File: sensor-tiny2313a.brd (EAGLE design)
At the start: 54 x 39 mm, 36 parts, among them IC1 TINY2313-*S*, M1 NRF24L01P-M, M2 DHT22-NP, Q2 IRLML2502, U1 MCP1640C, X1 I2C, X2 serial

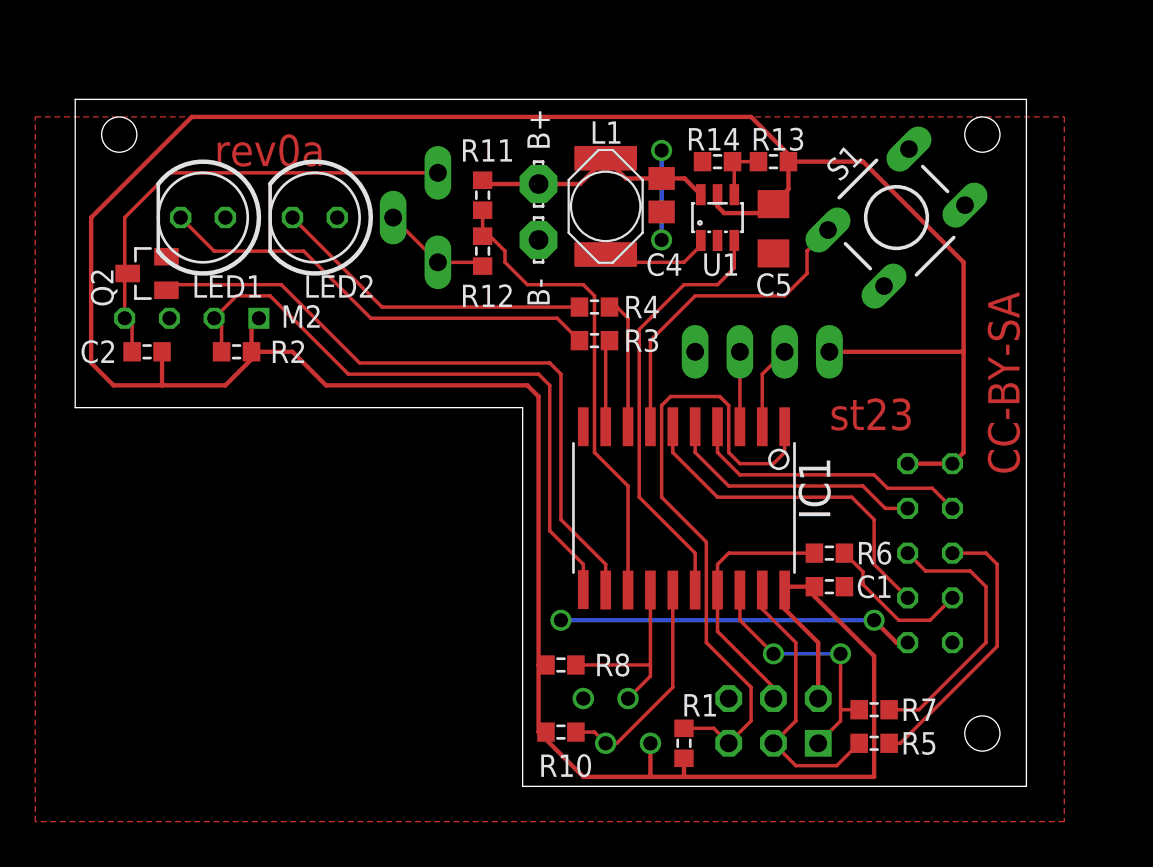
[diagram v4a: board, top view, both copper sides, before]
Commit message: renamed ic1->u1, u1->u2
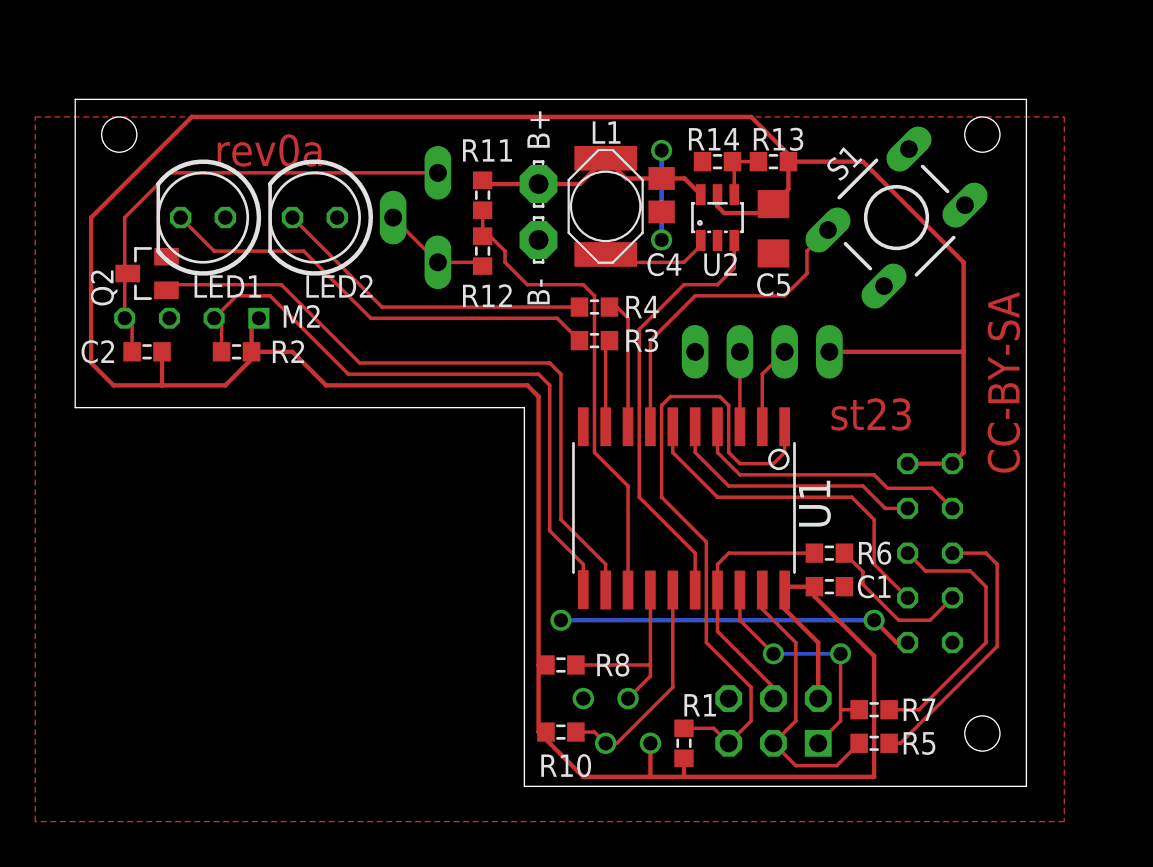
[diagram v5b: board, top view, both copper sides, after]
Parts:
- removed IC1: TINY2313-*S*, avr-7:SO20L$
- added U2: MCP1640C, karlnet-parts:SOT23-6
- U1: value MCP1640C -> TINY2313-*S*; device karlnet-parts:SOT23-6 -> avr-7:SO20L$
- moved U1 16.6 mm to (35.6, 17.8), turned to 180 degrees
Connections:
- net !RESET: now also U1.1; no longer IC1.1
- net AIN1: now also U1.13; no longer IC1.13
- net DHTON: now also U1.12; no longer IC1.12
- net DI: now also U1.17; no longer IC1.17
- net DO: now also U1.18; no longer IC1.18
- net GND: now also U1.10, U2.2; no longer IC1.10, U1.2
- net ICP1: now also U1.11; no longer IC1.11
- net LED1: now also U1.9; no longer IC1.9
- net LED2: now also U1.8; no longer IC1.8
- net N$8: now also U2.1; no longer U1.1
- net N$9: now also U2.4; no longer U1.4
- net PWRON: now also U1.16, U2.3; no longer IC1.16, U1.3
- net RFCE: now also U1.4; no longer IC1.4
- net RFCSN: now also U1.5; no longer IC1.5
- net RFIRQ: now also U1.6; no longer IC1.6
- net RXD: now also U1.2; no longer IC1.2
- net SCK: now also U1.19; no longer IC1.19
- net SCL: now also U1.15; no longer IC1.15
- net SDA: now also U1.14; no longer IC1.14
- net SW1: now also U1.7; no longer IC1.7
- net TXD: now also U1.3; no longer IC1.3
- net VBAT: now also U2.6; no longer U1.6
- net VCC: now also U1.20, U2.5; no longer IC1.20, U1.5
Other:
- outline, holes or cut-outs redrawn
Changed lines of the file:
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@@
 <layer number="44" name="Drills" color="7" fill="1" visible="no" active="yes"/>
 <layer number="45" name="Holes" color="7" fill="1" visible="no" active="yes"/>
-<layer number="46" name="Milling" color="3" fill="1" visible="no" active="yes"/>
+<layer number="46" name="Milling" color="3" fill="1" visible="yes" active="yes"/>
 <layer number="47" name="Measures" color="7" fill="1" visible="no" active="yes"/>
 <layer number="48" name="Document" color="7" fill="1" visible="no" active="yes"/>
@@
 <board>
 <plain>
-<wire x1="26.4" y1="2" x2="55" y2="2" width="0" layer="20"/>
+<wire x1="26.5" y1="2" x2="55" y2="2" width="0" layer="20"/>
 <wire x1="55" y1="2" x2="55" y2="41" width="0" layer="20"/>
 <wire x1="55" y1="41" x2="1" y2="41" width="0" layer="20"/>
 <wire x1="1" y1="41" x2="1" y2="23.5" width="0" layer="20"/>
-<wire x1="1" y1="23.5" x2="26.4" y2="23.5" width="0" layer="20"/>
-<wire x1="26.4" y1="23.5" x2="26.4" y2="2" width="0" layer="20"/>
+<wire x1="1" y1="23.5" x2="26.5" y2="23.5" width="0" layer="20"/>
+<wire x1="26.5" y1="23.5" x2="26.5" y2="2" width="0" layer="20"/>
 <hole x="52.5" y="5" drill="2"/>
 <hole x="52.5" y="39" drill="2"/>
@@
 <attribute name="VALUE" x="46.99" y="8.89" size="1.27" layer="27" rot="R180"/>
 </element>
-<element name="IC1" library="avr-7" package="SO20L$" value="TINY2313-*S*" x="35.56" y="17.78" smashed="yes" rot="R180">
-<attribute name="NAME" x="42.0878" y="20.701" size="1.778" layer="25" ratio="10" rot="R270"/>
+<element name="U1" library="avr-7" package="SO20L$" value="TINY2313-*S*" x="35.56" y="17.78" smashed="yes" rot="R180">
+<attribute name="NAME" x="42.0878" y="19.558" size="1.778" layer="25" ratio="10" rot="R270"/>
 <attribute name="VALUE" x="45.72" y="18.542" size="1.778" layer="27" ratio="10" rot="R180"/>
 </element>
@@
 <attribute name="VALUE" x="27.051" y="36.195" size="0.0254" layer="27" rot="R90"/>
 </element>
-<element name="U1" library="karlnet-parts" package="SOT23-6" value="MCP1640C" x="37.465" y="34.29" smashed="yes">
+<element name="U2" library="karlnet-parts" package="SOT23-6" value="MCP1640C" x="37.465" y="34.29" smashed="yes">
 <attribute name="NAME" x="36.576" y="30.988" size="1.27" layer="25"/>
 <attribute name="VALUE" x="35.56" y="30.861" size="1.27" layer="27"/>
@@
 <signals>
 <signal name="SCK">
-<contactref element="IC1" pad="19"/>
+<contactref element="U1" pad="19"/>
 <contactref element="R5" pad="1"/>
 <contactref element="ISP" pad="3"/>
@@
 <contactref element="C1" pad="2"/>
 <contactref element="ISP" pad="6"/>
-<contactref element="IC1" pad="10"/>
+<contactref element="U1" pad="10"/>
 <contactref element="S1" pad="3"/>
-<contactref element="IC1" pad="10"/>
+<contactref element="U1" pad="10"/>
 <contactref element="M1" pad="GND_A"/>
 <contactref element="M1" pad="GND_B"/>
@@
 <vertex x="-1.27" y="0"/>
 </polygon>
-<contactref element="U1" pad="2"/>
+<contactref element="U2" pad="2"/>
 <contactref element="C4" pad="2"/>
 <contactref element="B-" pad="MP"/>
@@
 <contactref element="ISP" pad="2"/>
 <contactref element="C1" pad="1"/>
-<contactref element="IC1" pad="20"/>
-<contactref element="IC1" pad="20"/>
+<contactref element="U1" pad="20"/>
+<contactref element="U1" pad="20"/>
 <contactref element="M1" pad="VCC_B"/>
 <contactref element="M1" pad="VCC_A"/>
 <contactref element="M1" pad="VCC_B"/>
 <contactref element="M1" pad="VCC_A"/>
-<contactref element="U1" pad="5"/>
+<contactref element="U2" pad="5"/>
 <contactref element="C5" pad="1"/>
 <contactref element="R13" pad="1"/>
@@
 <signal name="DHTON">
 <contactref element="Q2" pad="1"/>
-<contactref element="IC1" pad="12"/>
+<contactref element="U1" pad="12"/>
 <wire x1="28.575" y1="17.145" x2="31.115" y2="14.605" width="0.2" layer="1"/>
 <wire x1="31.115" y1="14.605" x2="31.115" y2="13.1445" width="0.2" layer="1"/>
@@
 </signal>
 <signal name="AIN1">
-<contactref element="IC1" pad="13"/>
+<contactref element="U1" pad="13"/>
 <contactref element="R11" pad="2"/>
 <contactref element="R12" pad="1"/>
@@
 </signal>
 <signal name="!RESET">
-<contactref element="IC1" pad="1"/>
+<contactref element="U1" pad="1"/>
 <contactref element="R1" pad="2"/>
 <contactref element="ISP" pad="5"/>
@@
 <signal name="RFCE">
 <contactref element="M1" pad="CE"/>
-<contactref element="IC1" pad="4"/>
+<contactref element="U1" pad="4"/>
 <wire x1="50.8" y1="17.78" x2="49.657" y2="18.923" width="0.2" layer="1"/>
 <wire x1="49.657" y1="18.923" x2="47.117" y2="18.923" width="0.2" layer="1"/>
@@
 </signal>
 <signal name="LED1">
-<contactref element="IC1" pad="9"/>
+<contactref element="U1" pad="9"/>
 <contactref element="R3" pad="1"/>
 <wire x1="31.115" y1="22.4155" x2="31.115" y2="27.09" width="0.2" layer="1"/>
@@
 <signal name="ICP1">
 <contactref element="R2" pad="2"/>
-<contactref element="IC1" pad="11"/>
+<contactref element="U1" pad="11"/>
 <contactref element="M2" pad="2"/>
 <wire x1="8.89" y1="28.575" x2="9.31" y2="28.155" width="0.2" layer="1"/>
@@
 </signal>
 <signal name="DO">
-<contactref element="IC1" pad="18"/>
+<contactref element="U1" pad="18"/>
 <contactref element="R7" pad="2"/>
 <contactref element="ISP" pad="1"/>
@@
 </signal>
 <signal name="DI">
-<contactref element="IC1" pad="17"/>
+<contactref element="U1" pad="17"/>
 <contactref element="R6" pad="1"/>
 <contactref element="ISP" pad="4"/>
@@
 <signal name="RFCSN">
 <contactref element="M1" pad="CSN"/>
-<contactref element="IC1" pad="5"/>
+<contactref element="U1" pad="5"/>
 <wire x1="48.26" y1="17.78" x2="46.99" y2="17.78" width="0.2" layer="1"/>
 <wire x1="46.99" y1="17.78" x2="45.72" y2="19.05" width="0.2" layer="1"/>
@@
 </signal>
 <signal name="SW1">
-<contactref element="IC1" pad="7"/>
+<contactref element="U1" pad="7"/>
 <contactref element="S1" pad="1"/>
 <wire x1="33.655" y1="22.4155" x2="33.655" y2="27.305" width="0.2" layer="1"/>
@@
 <signal name="N$8">
 <contactref element="L1" pad="1"/>
-<contactref element="U1" pad="1"/>
+<contactref element="U2" pad="1"/>
 <wire x1="36.515" y1="32.99" x2="36.515" y2="32.705" width="0.2" layer="1"/>
 <wire x1="36.515" y1="32.705" x2="35.56" y2="31.75" width="0.2" layer="1"/>
@@
 <contactref element="R13" pad="2"/>
 <contactref element="R14" pad="2"/>
-<contactref element="U1" pad="4"/>
+<contactref element="U2" pad="4"/>
 <wire x1="38.415" y1="35.59" x2="38.415" y2="37.365" width="0.2" layer="1"/>
 <wire x1="38.415" y1="37.365" x2="38.315" y2="37.465" width="0.2" layer="1"/>
@@
 </signal>
 <signal name="VBAT" class="1">
-<contactref element="U1" pad="6"/>
+<contactref element="U2" pad="6"/>
 <contactref element="L1" pad="2"/>
 <contactref element="C4" pad="1"/>
@@
 </signal>
 <signal name="PWRON">
-<contactref element="U1" pad="3"/>
-<contactref element="IC1" pad="16"/>
+<contactref element="U2" pad="3"/>
+<contactref element="U1" pad="16"/>
 <wire x1="38.415" y1="32.99" x2="38.415" y2="31.43" width="0.2" layer="1"/>
 <wire x1="33.02" y1="18.415" x2="36.195" y2="15.24" width="0.2" layer="1"/>
@@
 <signal name="RFIRQ">
 <contactref element="M1" pad="IRQ"/>
-<contactref element="IC1" pad="6"/>
+<contactref element="U1" pad="6"/>
 <wire x1="45.085" y1="18.415" x2="37.465" y2="18.415" width="0.2" layer="1"/>
 <wire x1="45.085" y1="18.415" x2="46.355" y2="17.145" width="0.2" layer="1"/>
@@
 </signal>
 <signal name="LED2">
-<contactref element="IC1" pad="8"/>
+<contactref element="U1" pad="8"/>
 <contactref element="R4" pad="1"/>
 <wire x1="32.385" y1="22.4155" x2="32.385" y2="28.575" width="0.2" layer="1"/>
@@
 </signal>
 <signal name="TXD">
-<contactref element="IC1" pad="3"/>
+<contactref element="U1" pad="3"/>
 <contactref element="X2" pad="3"/>
 <wire x1="38.735" y1="22.4155" x2="38.735" y2="26.67" width="0.2" layer="1"/>
 </signal>
 <signal name="RXD">
-<contactref element="IC1" pad="2"/>
+<contactref element="U1" pad="2"/>
 <contactref element="X2" pad="2"/>
 <wire x1="40.005" y1="22.4155" x2="40.005" y2="25.4" width="0.2" layer="1"/>
@@
 </signal>
 <signal name="SDA">
-<contactref element="IC1" pad="14"/>
+<contactref element="U1" pad="14"/>
 <contactref element="R8" pad="2"/>
 <contactref element="X1" pad="2"/>
@@
 </signal>
 <signal name="SCL">
-<contactref element="IC1" pad="15"/>
+<contactref element="U1" pad="15"/>
 <contactref element="R10" pad="2"/>
 <contactref element="X1" pad="3"/>
@@
 </signal>
 </signals>
-<errors>
-</errors>
 </board>
 </drawing>

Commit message: gnd plane reshaped
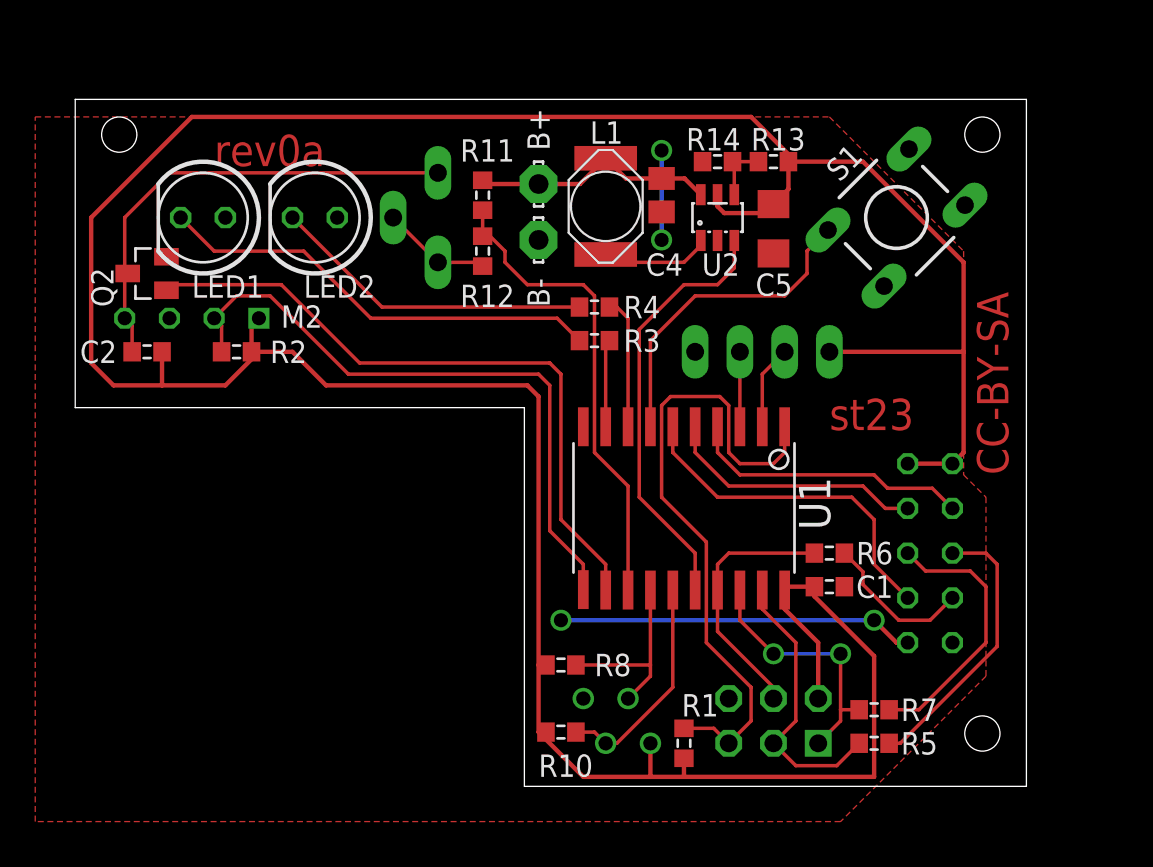
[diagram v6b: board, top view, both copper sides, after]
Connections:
- net GND: no longer S1.4
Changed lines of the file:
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@@
 <layer number="14" name="Route14" color="1" fill="6" visible="no" active="no"/>
 <layer number="15" name="Route15" color="4" fill="6" visible="no" active="no"/>
-<layer number="16" name="Bottom" color="1" fill="1" visible="no" active="yes"/>
+<layer number="16" name="Bottom" color="1" fill="1" visible="yes" active="yes"/>
 <layer number="17" name="Pads" color="2" fill="1" visible="yes" active="yes"/>
 <layer number="18" name="Vias" color="2" fill="1" visible="yes" active="yes"/>
@@
 <layer number="20" name="Dimension" color="15" fill="1" visible="yes" active="yes"/>
 <layer number="21" name="tPlace" color="7" fill="1" visible="yes" active="yes"/>
-<layer number="22" name="bPlace" color="7" fill="1" visible="no" active="yes"/>
+<layer number="22" name="bPlace" color="7" fill="1" visible="yes" active="yes"/>
 <layer number="23" name="tOrigins" color="15" fill="1" visible="yes" active="yes"/>
-<layer number="24" name="bOrigins" color="15" fill="1" visible="no" active="yes"/>
+<layer number="24" name="bOrigins" color="15" fill="1" visible="yes" active="yes"/>
 <layer number="25" name="tNames" color="7" fill="1" visible="yes" active="yes"/>
 <layer number="26" name="bNames" color="7" fill="1" visible="no" active="yes"/>
@@
 <text x="43.815" y="22.225" size="1.778" layer="1" font="vector" ratio="12">&gt;BN</text>
 <text x="8.89" y="37.211" size="1.778" layer="1" ratio="12">&gt;BR</text>
-<text x="54.61" y="19.685" size="1.778" layer="1" ratio="12" rot="R90">CC-BY-SA</text>
+<text x="53.975" y="19.685" size="1.778" layer="1" ratio="12" rot="R90">CC-BY-SA</text>
 <dimension x1="1" y1="41" x2="0.6" y2="23.5" x3="-5.2" y3="32.25" textsize="1.778" textratio="12" layer="47" dtype="vertical"/>
 <dimension x1="26.4" y1="2" x2="26.4" y2="23.5" x3="-9.6" y3="12.75" textsize="1.778" textratio="12" layer="47" dtype="vertical"/>
@@
 <polygon width="0.25" layer="1">
 <vertex x="-1.27" y="40.005"/>
-<vertex x="57.15" y="40.005"/>
-<vertex x="57.15" y="0"/>
+<vertex x="43.815" y="40.005"/>
+<vertex x="51.435" y="32.385"/>
+<vertex x="51.435" y="19.685"/>
+<vertex x="52.705" y="18.415"/>
+<vertex x="52.705" y="8.255"/>
+<vertex x="44.45" y="0"/>
 <vertex x="-1.27" y="0"/>
 </polygon>
@@
 <wire x1="46.355" y1="11.43" x2="28.575" y2="11.43" width="0.25" layer="16"/>
 <via x="28.575" y="11.43" extent="1-16" drill="0.8" shape="octagon"/>
-<contactref element="S1" pad="4"/>
 </signal>
 <signal name="VCC" class="1">

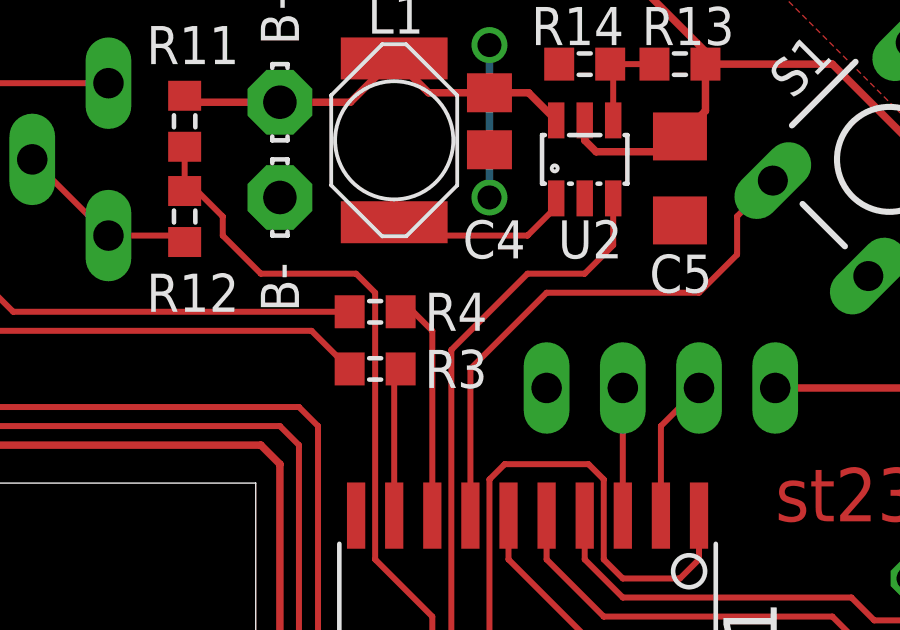
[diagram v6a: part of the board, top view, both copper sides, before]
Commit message: pulldown for boostup enable line
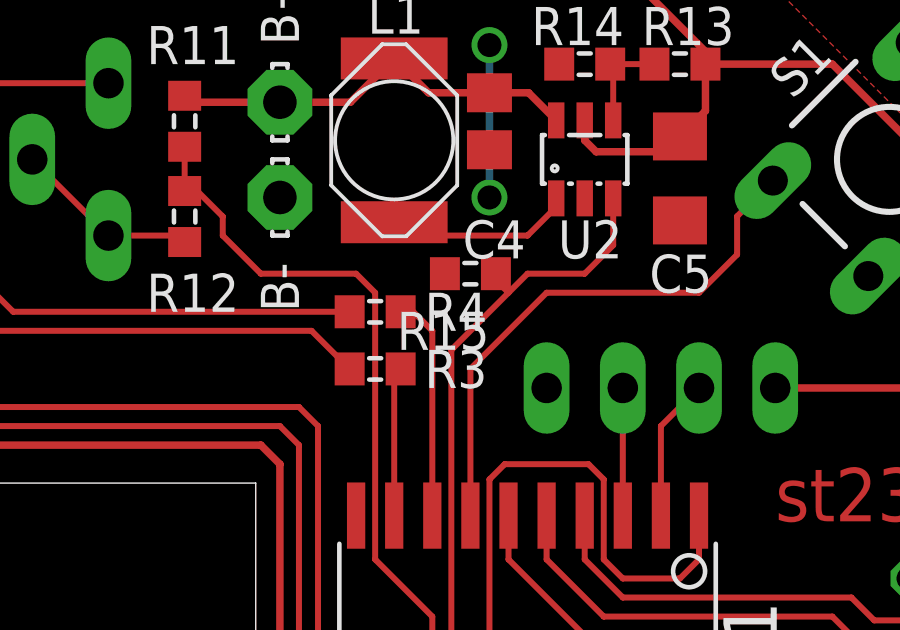
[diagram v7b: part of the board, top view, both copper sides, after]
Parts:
- added R15: 10k, rcl:R0603
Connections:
- net GND: now also R15.2
- net PWRON: now also R15.1
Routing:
- net PWRON: track 24.5 -> 25.6 mm
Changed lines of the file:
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@@
 <setting verticaltext="up"/>
 </settings>
-<grid distance="0.635" unitdist="mm" unit="mm" style="lines" multiple="1" display="yes" altdistance="5" altunitdist="mil" altunit="mic"/>
+<grid distance="0.635" unitdist="mm" unit="mm" style="lines" multiple="1" display="yes" altdistance="0.127" altunitdist="mm" altunit="mm"/>
 <layers>
 <layer number="1" name="Top" color="4" fill="1" visible="yes" active="yes"/>
@@
 <element name="U$3" library="creative-commons" package="BY_TPLACE_HS" value="BY-TPLACE-HS" x="26.035" y="24.13" rot="MR0"/>
 <element name="U$4" library="creative-commons" package="SA_TPLACE_HS" value="SA-TPLACE-HALF" x="20.32" y="24.13" rot="MR0"/>
+<element name="R15" library="rcl" package="R0603" value="10k" x="33.655" y="30.48" rot="R180"/>
 </elements>
 <signals>
@@
 <wire x1="46.355" y1="11.43" x2="28.575" y2="11.43" width="0.25" layer="16"/>
 <via x="28.575" y="11.43" extent="1-16" drill="0.8" shape="octagon"/>
+<contactref element="R15" pad="2"/>
 </signal>
 <signal name="VCC" class="1">
@@
 <wire x1="36.195" y1="15.24" x2="36.195" y2="13.1445" width="0.2" layer="1"/>
 <wire x1="33.02" y1="18.415" x2="33.02" y2="27.94" width="0.2" layer="1"/>
-<wire x1="33.02" y1="27.94" x2="35.56" y2="30.48" width="0.2" layer="1"/>
+<wire x1="33.02" y1="27.94" x2="34.925" y2="29.845" width="0.2" layer="1"/>
+<wire x1="34.925" y1="29.845" x2="35.56" y2="30.48" width="0.2" layer="1"/>
 <wire x1="35.56" y1="30.48" x2="37.465" y2="30.48" width="0.2" layer="1"/>
 <wire x1="37.465" y1="30.48" x2="38.415" y2="31.43" width="0.2" layer="1"/>
+<contactref element="R15" pad="1"/>
+<wire x1="34.505" y1="30.48" x2="34.29" y2="30.48" width="0.2" layer="1"/>
+<wire x1="34.29" y1="30.48" x2="34.925" y2="29.845" width="0.2" layer="1"/>
 </signal>
 <signal name="RFIRQ">
